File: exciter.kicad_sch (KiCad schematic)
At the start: 36 parts, among them U7 CC1200, X1 40MHz

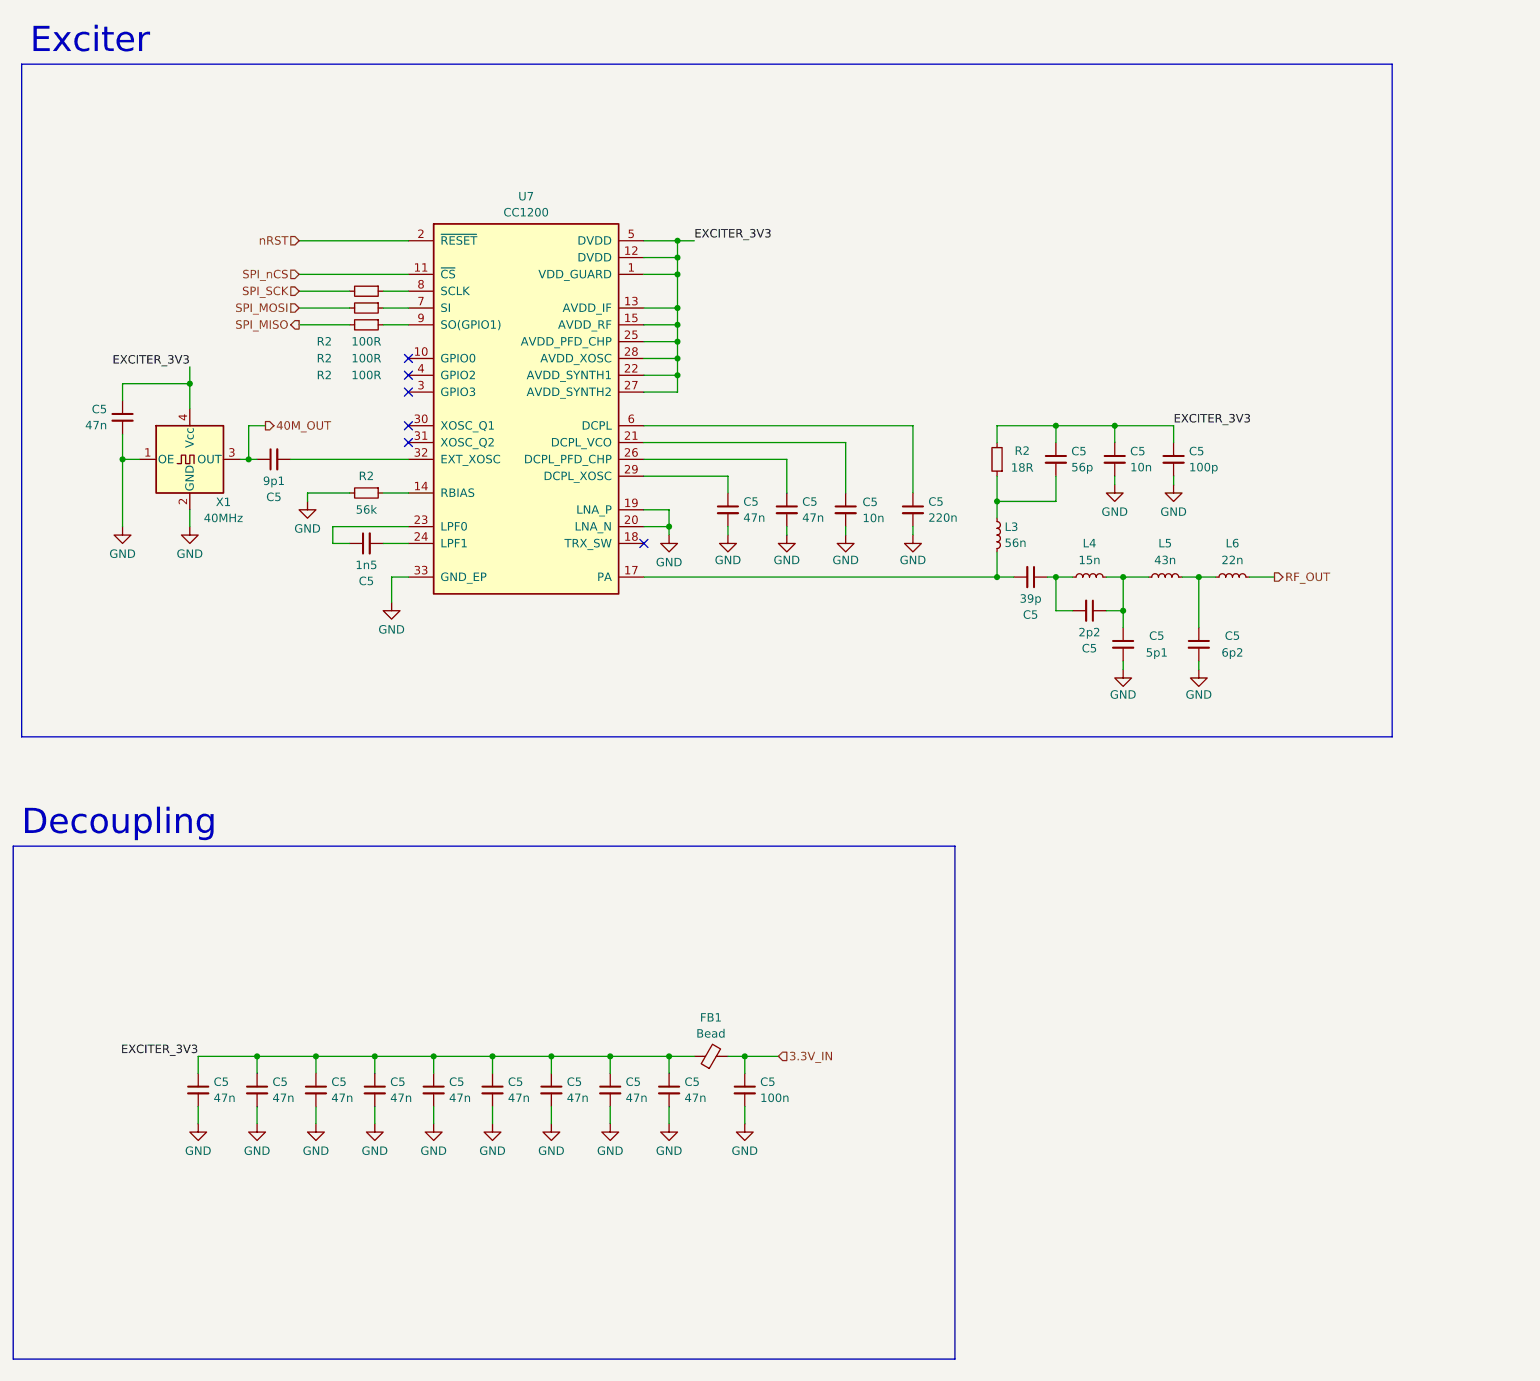
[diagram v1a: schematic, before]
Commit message: `PWR_FLAG`, ERC cleanup
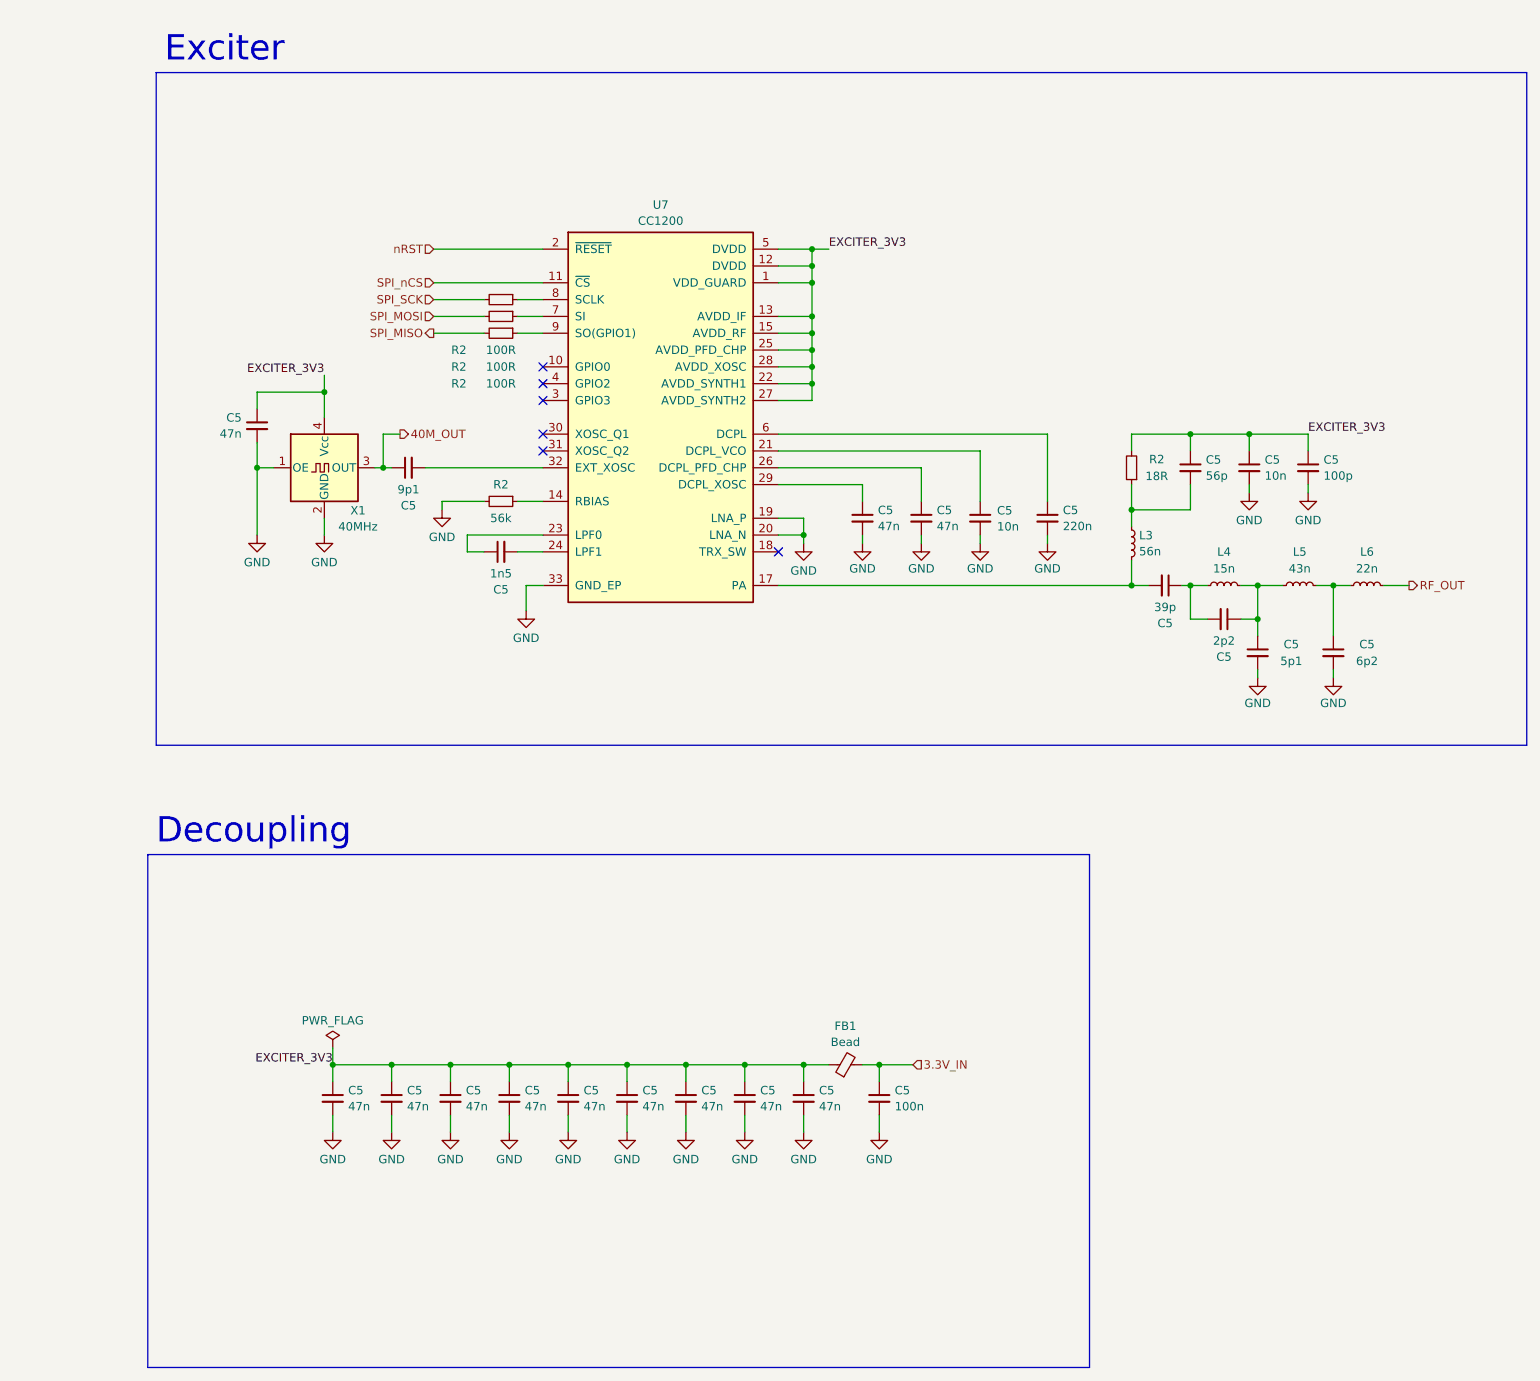
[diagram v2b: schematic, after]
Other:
- moved on the sheet: C5, FB1, L3, L4, L5, L6, R2, U7, X1

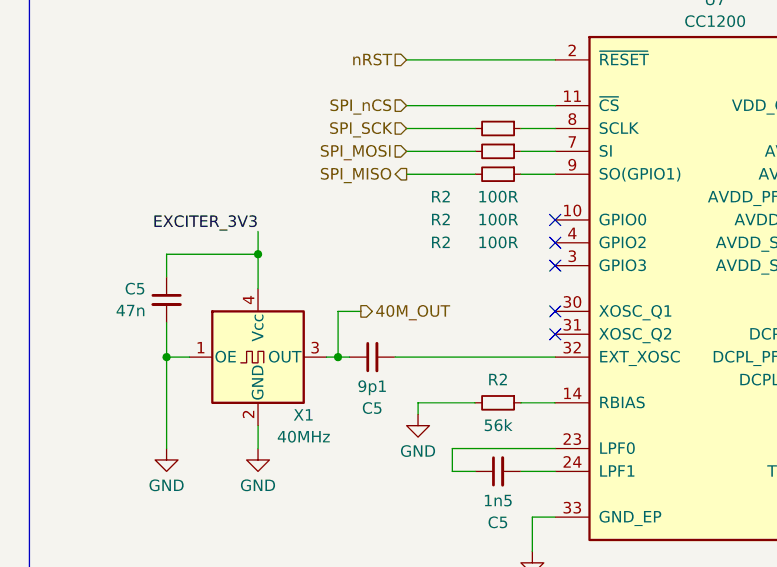
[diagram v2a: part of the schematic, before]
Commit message: TP updates, temp sensor added
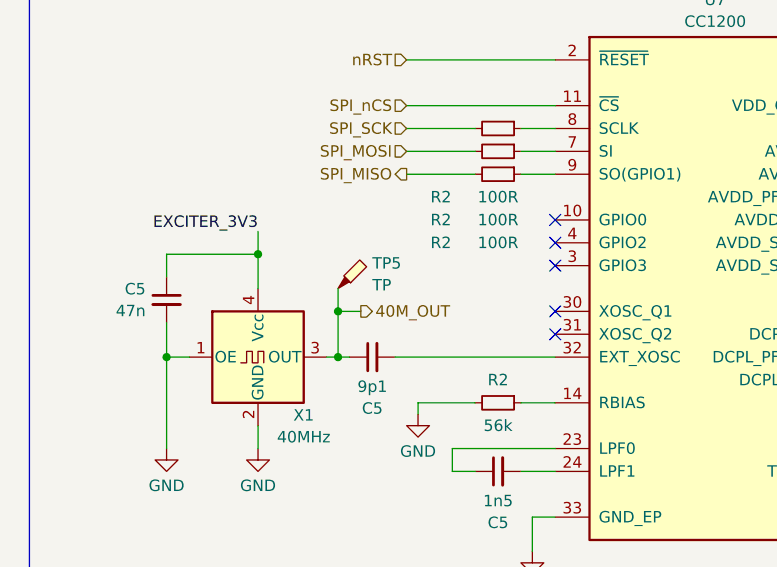
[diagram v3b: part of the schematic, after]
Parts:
- added TP5: TP, TestPoint:TestPoint_Pad_D1.5mm, symbol Connector:TestPoint_Probe
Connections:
- net 40M_OUT: now also TP5.1

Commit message: date update
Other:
- title: M17 Remote Radio Unit - RF board -> Remote Radio Unit - RF board
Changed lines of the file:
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@@
   (paper "A3")
   (title_block
-    (title "M17 Remote Radio Unit - RF board")
-    (date "28-10-2023")
+    (title "Remote Radio Unit - RF board")
+    (date "30-10-2023")
     (rev "A")
     (company "M17 Project")

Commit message: MPN/PN update
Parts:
- C5: MPN (none) -> C0603C223K4RACTU
- C5: MPN (none) -> C0603C473K5RACTU
- C5: MPN (none) -> 0603N560F500CT
- C5: MPN (none) -> C0603C103K5RAC7081
- C5: MPN (none) -> CL10C390JB81PNC
- C5: MPN (none) -> GRM1885C1H6R2BA01D
- C5: MPN (none) -> GRM1885C1H9R1BA01D
- C5: MPN (none) -> C0603C104M5RAC7411
- C5: MPN (none) -> CC0603BRNPO9BN2R2
- C5: MPN (none) -> GRM1885C1H152JA01D
- C5: MPN (none) -> CC0603CRNPO9BN5R1
- C5: MPN (none) -> VJ0603A101JXAPW1BC
- FB1: MPN (none) -> BLM18KG601SH1D
- L3: MPN (none) -> LQW18AS56NG00D; PN (none) -> LQW18AS56NG00D
- L4: MPN (none) -> LQW18AS15NG00D; PN (none) -> LQW18AS15NG00D
- L5: MPN (none) -> LQW18AN43NJ00D; PN (none) -> LQW18AN43NJ00D
- L6: MPN (none) -> LQW18AN22NG00D; PN (none) -> LQW18AN22NG00D
- R2: MPN (none) -> CRCW0603100RFKECC; PN (none) -> CRCW0603100RFKECC
- R2: MPN (none) -> CRGCQ0603F56K; PN (none) -> CRGCQ0603F56K
- R2: MPN (none) -> RC0603FR-0718RL; PN RC0603FR-0718RL -> RC0603FR-0718RL
- TP5: MPN (none) -> -
- U7: MPN (none) -> CC1200RHBR
- X1: MPN (none) -> FT2MNTUM-40.0-T1
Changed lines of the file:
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@@
+      (effects (font (size 1.27 1.27)) hide)
+    )
+    (property "MPN" "C0603C223K4RACTU" (at 237.49 116.84 0)
       (effects (font (size 1.27 1.27)) hide)
     )
@@
       (effects (font (size 1.27 1.27)) hide)
     )
-    (property "PN" "" (at 154.94 88.9 0)
+    (property "PN" "CRCW0603100RFKECC" (at 154.94 88.9 0)
+      (effects (font (size 1.27 1.27)) hide)
+    )
+    (property "MPN" "CRCW0603100RFKECC" (at 154.94 88.9 0)
       (effects (font (size 1.27 1.27)) hide)
     )
@@
       (effects (font (size 1.27 1.27)) hide)
     )
+    (property "MPN" "LQW18AN22NG00D" (at 285.75 127 0)
+      (effects (font (size 1.27 1.27)) hide)
+    )
+    (property "PN" "LQW18AN22NG00D" (at 285.75 127 0)
+      (effects (font (size 1.27 1.27)) hide)
+    )
     (pin "1")
     (pin "2")
@@
       (effects (font (size 1.27 1.27)) hide)
     )
+    (property "MPN" "LQW18AS56NG00D" (at 250.19 120.65 0)
+      (effects (font (size 1.27 1.27)) hide)
+    )
+    (property "PN" "LQW18AS56NG00D" (at 250.19 120.65 0)
+      (effects (font (size 1.27 1.27)) hide)
+    )
     (pin "1")
     (pin "2")
@@
       (effects (font (size 1.27 1.27)) hide)
     )
+    (property "MPN" "C0603C473K5RACTU" (at 173.99 204.47 0)
+      (effects (font (size 1.27 1.27)) hide)
+    )
     (pin "1")
     (pin "2")
@@
     )
     (property "PN" "FT2MNTUM-40.0-T1" (at 128.27 109.22 0)
+      (effects (font (size 1.27 1.27)) hide)
+    )
+    (property "MPN" "FT2MNTUM-40.0-T1" (at 128.27 109.22 0)
       (effects (font (size 1.27 1.27)) hide)
     )
@@
       (effects (font (size 1.27 1.27)) hide)
     )
+    (property "MPN" "BLM18KG601SH1D" (at 207.01 199.39 0)
+      (effects (font (size 1.27 1.27)) hide)
+    )
     (pin "1")
     (pin "2")
@@
       (effects (font (size 1.27 1.27)) hide)
     )
+    (property "MPN" "0603N560F500CT" (at 259.08 109.22 0)
+      (effects (font (size 1.27 1.27)) hide)
+    )
     (pin "1")
     (pin "2")
@@
     )
     (property "PN" "C0603C473K5RACTU" (at 156.21 204.47 0)
+      (effects (font (size 1.27 1.27)) hide)
+    )
+    (property "MPN" "C0603C473K5RACTU" (at 156.21 204.47 0)
       (effects (font (size 1.27 1.27)) hide)
     )
@@
       (effects (font (size 1.27 1.27)) hide)
     )
+    (property "MPN" "C0603C473K5RACTU" (at 200.66 204.47 0)
+      (effects (font (size 1.27 1.27)) hide)
+    )
     (pin "1")
     (pin "2")
@@
     )
     (property "PN" "-" (at 137.16 101.6 0)
+      (effects (font (size 1.27 1.27)) hide)
+    )
+    (property "MPN" "-" (at 137.16 101.6 0)
       (effects (font (size 1.27 1.27)) hide)
     )
@@
       (effects (font (size 1.27 1.27)) hide)
     )
+    (property "MPN" "C0603C473K5RACTU" (at 209.55 116.84 0)
+      (effects (font (size 1.27 1.27)) hide)
+    )
     (pin "1")
     (pin "2")
@@
       (effects (font (size 1.27 1.27)) hide)
     )
-    (property "PN" "" (at 154.94 114.3 0)
+    (property "PN" "CRGCQ0603F56K" (at 154.94 114.3 0)
+      (effects (font (size 1.27 1.27)) hide)
+    )
+    (property "MPN" "CRGCQ0603F56K" (at 154.94 114.3 0)
       (effects (font (size 1.27 1.27)) hide)
     )
@@
       (effects (font (size 1.27 1.27)) hide)
     )
+    (property "MPN" "C0603C473K5RACTU" (at 147.32 204.47 0)
+      (effects (font (size 1.27 1.27)) hide)
+    )
     (pin "1")
     (pin "2")
@@
       (effects (font (size 1.27 1.27)) hide)
     )
+    (property "MPN" "C0603C103K5RAC7081" (at 267.97 109.22 0)
+      (effects (font (size 1.27 1.27)) hide)
+    )
     (pin "1")
     (pin "2")
@@
       (effects (font (size 1.27 1.27)) hide)
     )
+    (property "MPN" "CL10C390JB81PNC" (at 255.27 127 0)
+      (effects (font (size 1.27 1.27)) hide)
+    )
     (pin "1")
     (pin "2")
@@
       (effects (font (size 1.27 1.27)) hide)
     )
-    (property "PN" "" (at 154.94 86.36 0)
+    (property "PN" "CRCW0603100RFKECC" (at 154.94 86.36 0)
+      (effects (font (size 1.27 1.27)) hide)
+    )
+    (property "MPN" "CRCW0603100RFKECC" (at 154.94 86.36 0)
       (effects (font (size 1.27 1.27)) hide)
     )
@@
       (effects (font (size 1.27 1.27)) hide)
     )
+    (property "MPN" "GRM1885C1H6R2BA01D" (at 280.67 137.16 0)
+      (effects (font (size 1.27 1.27)) hide)
+    )
     (pin "1")
     (pin "2")
@@
       (effects (font (size 1.27 1.27)) hide)
     )
+    (property "MPN" "GRM1885C1H9R1BA01D" (at 140.97 109.22 0)
+      (effects (font (size 1.27 1.27)) hide)
+    )
     (pin "1")
     (pin "2")
@@
     )
     (property "PN" "CC1200RHBR" (at 179.07 101.6 0)
+      (effects (font (size 1.27 1.27)) hide)
+    )
+    (property "MPN" "CC1200RHBR" (at 179.07 101.6 0)
       (effects (font (size 1.27 1.27)) hide)
     )
@@
       (effects (font (size 1.27 1.27)) hide)
     )
+    (property "MPN" "C0603C473K5RACTU" (at 191.77 204.47 0)
+      (effects (font (size 1.27 1.27)) hide)
+    )
     (pin "1")
     (pin "2")
@@
       (effects (font (size 1.27 1.27)) hide)
     )
+    (property "MPN" "C0603C104M5RAC7411" (at 212.09 204.47 0)
+      (effects (font (size 1.27 1.27)) hide)
+    )
     (pin "1")
     (pin "2")
@@
       (effects (font (size 1.27 1.27)) hide)
     )
+    (property "MPN" "CC0603BRNPO9BN2R2" (at 264.16 132.08 0)
+      (effects (font (size 1.27 1.27)) hide)
+    )
     (pin "1")
     (pin "2")
@@
       (effects (font (size 1.27 1.27)) hide)
     )
+    (property "MPN" "C0603C103K5RAC7081" (at 227.33 116.84 0)
+      (effects (font (size 1.27 1.27)) hide)
+    )
     (pin "1")
     (pin "2")
@@
       (effects (font (size 1.27 1.27)) hide)
     )
+    (property "MPN" "C0603C473K5RACTU" (at 129.54 204.47 0)
+      (effects (font (size 1.27 1.27)) hide)
+    )
     (pin "1")
     (pin "2")
@@
       (effects (font (size 1.27 1.27)) hide)
     )
+    (property "MPN" "C0603C473K5RACTU" (at 138.43 204.47 0)
+      (effects (font (size 1.27 1.27)) hide)
+    )
     (pin "1")
     (pin "2")
@@
       (effects (font (size 1.27 1.27)) hide)
     )
+    (property "MPN" "LQW18AN43NJ00D" (at 275.59 127 0)
+      (effects (font (size 1.27 1.27)) hide)
+    )
+    (property "PN" "LQW18AN43NJ00D" (at 275.59 127 0)
+      (effects (font (size 1.27 1.27)) hide)
+    )
     (pin "1")
     (pin "2")
@@
       (effects (font (size 1.27 1.27)) hide)
     )
+    (property "MPN" "LQW18AS15NG00D" (at 264.16 127 0)
+      (effects (font (size 1.27 1.27)) hide)
+    )
+    (property "PN" "LQW18AS15NG00D" (at 264.16 127 0)
+      (effects (font (size 1.27 1.27)) hide)
+    )
     (pin "1")
     (pin "2")
@@
       (effects (font (size 1.27 1.27)) hide)
     )
-    (property "PN" "" (at 154.94 83.82 0)
+    (property "PN" "CRCW0603100RFKECC" (at 154.94 83.82 0)
+      (effects (font (size 1.27 1.27)) hide)
+    )
+    (property "MPN" "CRCW0603100RFKECC" (at 154.94 83.82 0)
       (effects (font (size 1.27 1.27)) hide)
     )
@@
       (effects (font (size 1.27 1.27)) hide)
     )
+    (property "MPN" "GRM1885C1H152JA01D" (at 154.94 121.92 0)
+      (effects (font (size 1.27 1.27)) hide)
+    )
     (pin "1")
     (pin "2")
@@
       (effects (font (size 1.27 1.27)) hide)
     )
-    (property "PN" " RC0603FR-0718RL " (at 250.19 109.22 0)
+    (property "PN" "RC0603FR-0718RL" (at 250.19 109.22 0)
+      (effects (font (size 1.27 1.27)) hide)
+    )
+    (property "MPN" "RC0603FR-0718RL" (at 250.19 109.22 0)
       (effects (font (size 1.27 1.27)) hide)
     )
@@
       (effects (font (size 1.27 1.27)) hide)
     )
+    (property "MPN" "C0603C473K5RACTU" (at 165.1 204.47 0)
+      (effects (font (size 1.27 1.27)) hide)
+    )
     (pin "1")
     (pin "2")
@@
       (effects (font (size 1.27 1.27)) hide)
     )
+    (property "MPN" "CC0603CRNPO9BN5R1" (at 269.24 137.16 0)
+      (effects (font (size 1.27 1.27)) hide)
+    )
     (pin "1")
     (pin "2")
@@
       (effects (font (size 1.27 1.27)) hide)
     )
+    (property "MPN" "C0603C473K5RACTU" (at 218.44 116.84 0)
+      (effects (font (size 1.27 1.27)) hide)
+    )
     (pin "1")
     (pin "2")
@@
       (effects (font (size 1.27 1.27)) hide)
     )
+    (property "MPN" "C0603C473K5RACTU" (at 118.11 102.87 0)
+      (effects (font (size 1.27 1.27)) hide)
+    )
     (pin "1")
     (pin "2")
@@
       (effects (font (size 1.27 1.27)) hide)
     )
+    (property "MPN" "C0603C473K5RACTU" (at 182.88 204.47 0)
+      (effects (font (size 1.27 1.27)) hide)
+    )
     (pin "1")
     (pin "2")
@@
       (effects (font (size 1.27 1.27)) hide)
     )
+    (property "MPN" "VJ0603A101JXAPW1BC" (at 276.86 109.22 0)
+      (effects (font (size 1.27 1.27)) hide)
+    )
